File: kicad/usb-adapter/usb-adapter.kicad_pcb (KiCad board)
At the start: 2 copper layers, 17.2 x 40.9 mm, 3 parts, among them J1 USB-A plug, port A, J2 USB-A plug, port B, J3 To main board

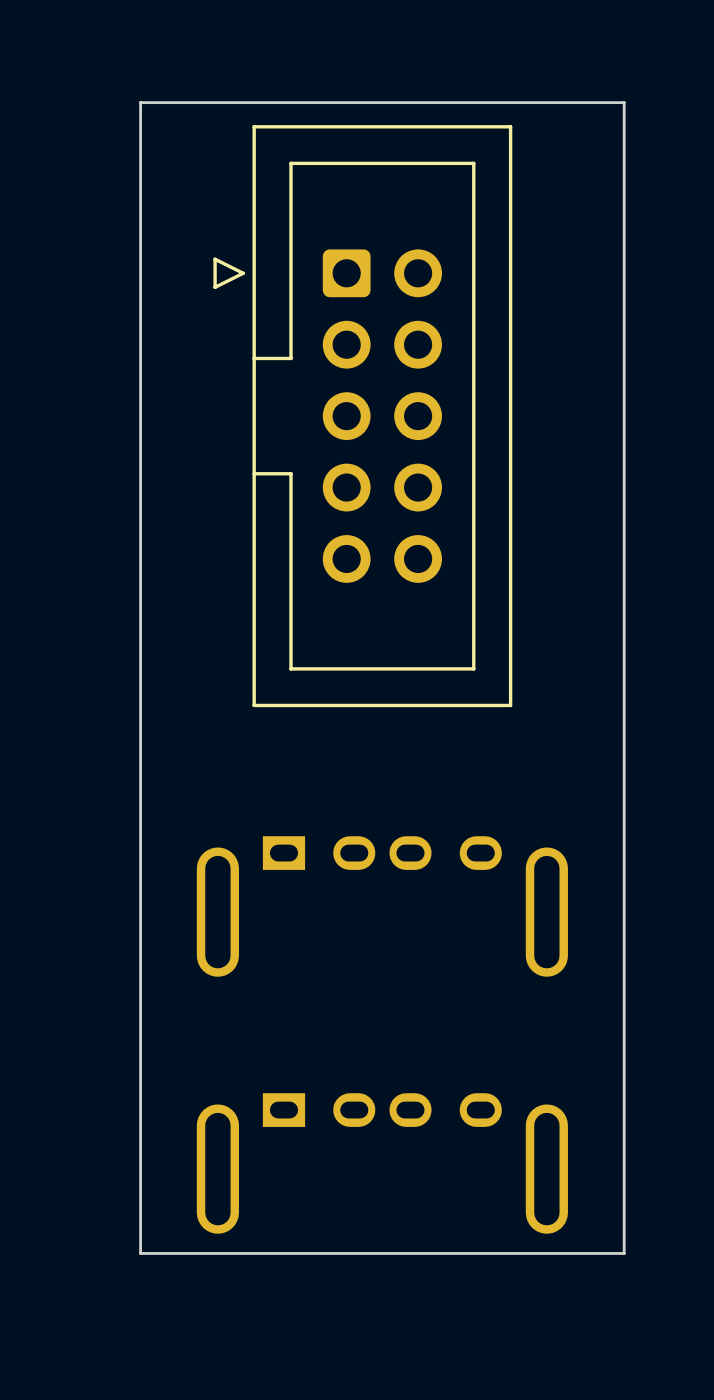
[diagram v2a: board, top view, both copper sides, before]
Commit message: USB adapters: routed board, plug placeholder, and both in Moirae's 3D
The adapter's plug tails sit on the plug's centre line (as routed); its
3D plug is a 12 x 4.5 x 15 mm box. The generator no longer overwrites the
hand-routed board. USBA1 / USBA2, board-only on the main board, stand the
adapter at the Pi 4's two USB stacks (27.0 and 9.0 up its port edge), plug
face 3 mm off the port faces.

Co-Authored-By: Claude Opus 5.5 <noreply@anthropic.com>
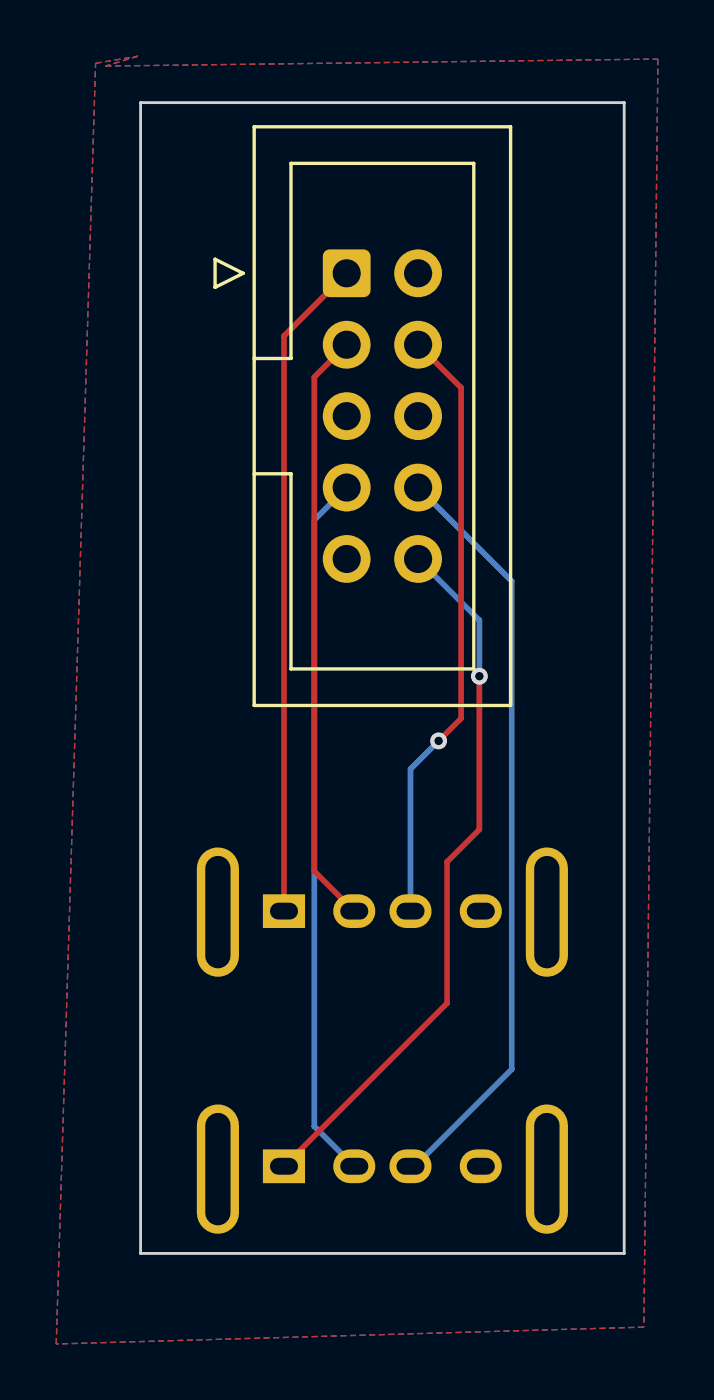
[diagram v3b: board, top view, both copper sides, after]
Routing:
- net /DP_B: track 0.00 -> 26.9 mm
- net /VBUS_B: track 0.00 -> 25.4 mm, vias 0 -> 1
- net /DM_B: track 0.00 -> 25.2 mm
- net /VBUS_A: track 0.00 -> 23.6 mm
- net /DP_A: track 0.00 -> 21.5 mm, vias 0 -> 1
- net /DM_A: track 0.00 -> 21.2 mm
- added copper zone on B.Cu, net GND
- added copper zone on F.Cu, net GND
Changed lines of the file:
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@@
 		)
 		(pad "1" thru_hole rect
-			(at -3.5 -2.1)
+			(at -3.5 -0.035)
 			(size 1.5 1.2)
 			(drill oval 1 0.6)
@@
 		)
 		(pad "2" thru_hole oval
-			(at -1 -2.1)
+			(at -1 -0.035)
 			(size 1.5 1.2)
 			(drill oval 1 0.6)
@@
 		)
 		(pad "3" thru_hole oval
-			(at 1 -2.1)
+			(at 1 -0.035)
 			(size 1.5 1.2)
 			(drill oval 1 0.6)
@@
 		)
 		(pad "4" thru_hole oval
-			(at 3.5 -2.1)
+			(at 3.5 -0.035)
 			(size 1.5 1.2)
 			(drill oval 1 0.6)
@@
 		)
 		(fp_text user "insert"
-			(at 0 -0.85 0)
+			(at 0 -1.2 0)
 			(layer "F.Fab")
 			(effects
@@
 		)
 		(pad "1" thru_hole rect
-			(at -3.5 -2.1)
+			(at -3.5 -0.1)
 			(size 1.5 1.2)
 			(drill oval 1 0.6)
@@
 		)
 		(pad "2" thru_hole oval
-			(at -1 -2.1)
+			(at -1 -0.1)
 			(size 1.5 1.2)
 			(drill oval 1 0.6)
@@
 		)
 		(pad "3" thru_hole oval
-			(at 1 -2.1)
+			(at 1 -0.1)
 			(size 1.5 1.2)
 			(drill oval 1 0.6)
@@
 		)
 		(pad "4" thru_hole oval
-			(at 3.5 -2.1)
+			(at 3.5 -0.1)
 			(size 1.5 1.2)
 			(drill oval 1 0.6)
@@
 			)
 		)
+	)
+	(segment
+		(start 98.73 60.769999)
+		(end 96.5 62.999999)
+		(width 0.2)
+		(layer "F.Cu")
+		(net "/VBUS_A")
+	)
+	(segment
+		(start 96.5 62.999999)
+		(end 96.5 83.455)
+		(width 0.2)
+		(layer "F.Cu")
+		(net "/VBUS_A")
+	)
+	(segment
+		(start 98.73 63.309999)
+		(end 97.58 64.459999)
+		(width 0.2)
+		(layer "F.Cu")
+		(net "/DM_A")
+	)
+	(segment
+		(start 97.58 64.459999)
+		(end 97.58 82.035)
+		(width 0.2)
+		(layer "F.Cu")
+		(net "/DM_A")
+	)
+	(segment
+		(start 97.58 82.035)
+		(end 99 83.455)
+		(width 0.2)
+		(layer "F.Cu")
+		(net "/DM_A")
+	)
+	(segment
+		(start 101.27 63.309999)
+		(end 102.8 64.839999)
+		(width 0.2)
+		(layer "F.Cu")
+		(net "/DP_A")
+	)
+	(segment
+		(start 102.8 64.839999)
+		(end 102.8 76.6)
+		(width 0.2)
+		(layer "F.Cu")
+		(net "/DP_A")
+	)
+	(segment
+		(start 102.8 76.6)
+		(end 102 77.4)
+		(width 0.2)
+		(layer "F.Cu")
+		(net "/DP_A")
+	)
+	(via
+		(at 102 77.4)
+		(size 0.6)
+		(drill 0.3)
+		(layers "F.Cu" "B.Cu")
+		(net "/DP_A")
+	)
+	(segment
+		(start 101 78.4)
+		(end 102 77.4)
+		(width 0.2)
+		(layer "B.Cu")
+		(net "/DP_A")
+	)
+	(segment
+		(start 101 83.455)
+		(end 101 78.4)
+		(width 0.2)
+		(layer "B.Cu")
+		(net "/DP_A")
+	)
+	(segment
+		(start 97.58 69.539999)
+		(end 97.58 91.11)
+		(width 0.2)
+		(layer "B.Cu")
+		(net "/DM_B")
+	)
+	(segment
+		(start 97.58 91.11)
+		(end 99 92.53)
+		(width 0.2)
+		(layer "B.Cu")
+		(net "/DM_B")
+	)
+	(segment
+		(start 98.73 68.389999)
+		(end 97.58 69.539999)
+		(width 0.2)
+		(layer "B.Cu")
+		(net "/DM_B")
+	)
+	(segment
+		(start 104.6 89.08)
+		(end 101.15 92.53)
+		(width 0.2)
+		(layer "B.Cu")
+		(net "/DP_B")
+	)
+	(segment
+		(start 101.27 68.389999)
+		(end 104.6 71.719999)
+		(width 0.2)
+		(layer "B.Cu")
+		(net "/DP_B")
+	)
+	(segment
+		(start 104.6 71.719999)
+		(end 104.6 89.08)
+		(width 0.2)
+		(layer "B.Cu")
+		(net "/DP_B")
+	)
+	(segment
+		(start 102.3 86.73)
+		(end 102.3 81.7)
+		(width 0.2)
+		(layer "F.Cu")
+		(net "/VBUS_B")
+	)
+	(segment
+		(start 96.5 92.53)
+		(end 102.3 86.73)
+		(width 0.2)
+		(layer "F.Cu")
+		(net "/VBUS_B")
+	)
+	(segment
+		(start 102.3 81.7)
+		(end 103.45 80.55)
+		(width 0.2)
+		(layer "F.Cu")
+		(net "/VBUS_B")
+	)
+	(segment
+		(start 103.45 80.55)
+		(end 103.45 75.1)
+		(width 0.2)
+		(layer "F.Cu")
+		(net "/VBUS_B")
+	)
+	(via
+		(at 103.45 75.1)
+		(size 0.6)
+		(drill 0.3)
+		(layers "F.Cu" "B.Cu")
+		(net "/VBUS_B")
+	)
+	(segment
+		(start 103.45 73.109999)
+		(end 103.45 75.1)
+		(width 0.2)
+		(layer "B.Cu")
+		(net "/VBUS_B")
+	)
+	(segment
+		(start 101.27 70.929999)
+		(end 103.45 73.109999)
+		(width 0.2)
+		(layer "B.Cu")
+		(net "/VBUS_B")
+	)
+	(zone
+		(net "GND")
+		(layers "F.Cu" "B.Cu")
+		(hatch edge 0.5)
+		(connect_pads
+			(clearance 0.5)
+		)
+		(min_thickness 0.25)
+		(fill yes
+			(thermal_gap 0.5)
+			(thermal_bridge_width 0.5)
+			(island_removal_mode 0)
+		)
+		(polygon
+			(pts
+				(xy 90.15 53.4) (xy 109.8 53.15) (xy 109.3 98.25) (xy 88.4 98.85) (xy 89.8 53.3) (xy 91.3 53.05)
+			)
+		)

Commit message: Pi USB ribbons routed on both boards; plug boxes in the adapter's 3D
Adapter J1 / J2 carry the 15 mm plug placeholder, and its STEP is
re-exported for Moirae. Pours refilled on both boards; the adapter's arc
approximation tightened so its pour clears the rounded edge.

Co-Authored-By: Claude Opus 5.5 <noreply@anthropic.com>
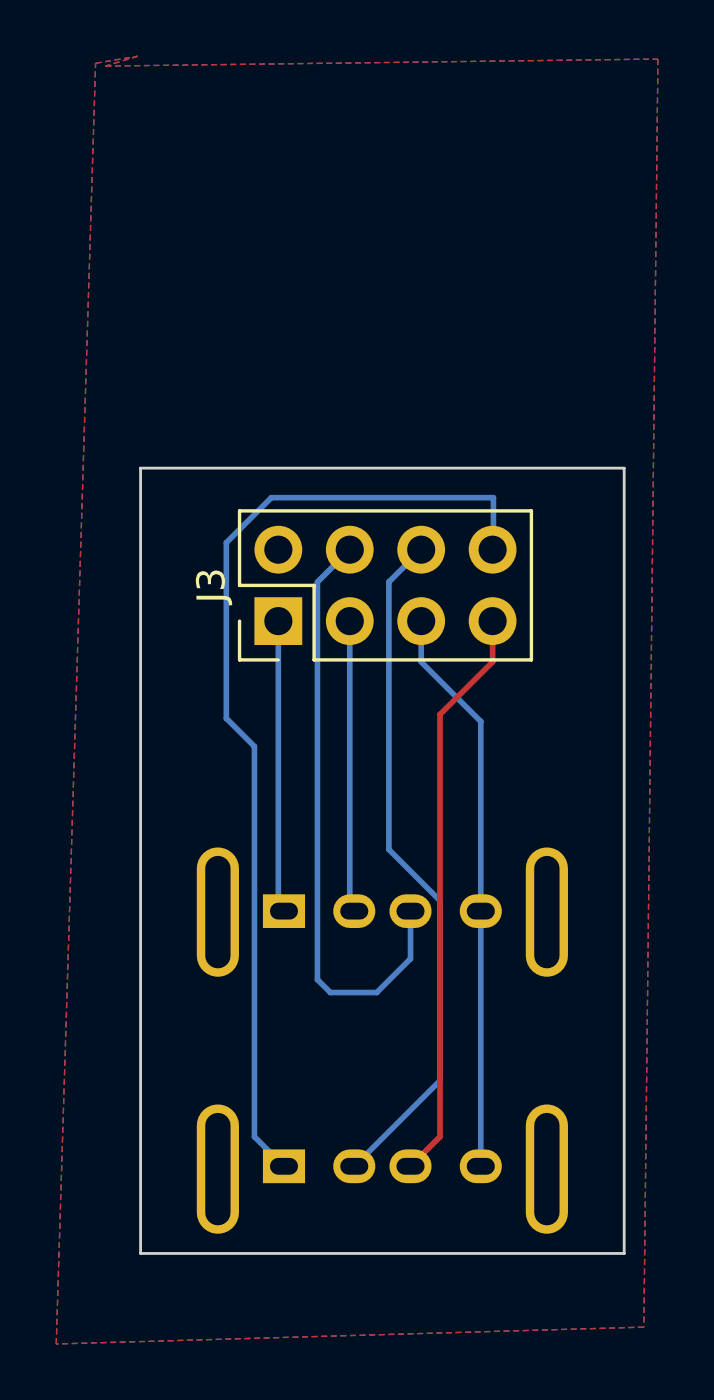
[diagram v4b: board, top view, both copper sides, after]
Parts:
- J3: footprint Connector_IDC:IDC-Header_2x05_P2.54mm_Vertical -> Connector_PinHeader_2.54mm:PinHeader_2x04_P2.54mm_Vertical
- moved J3 12.6 mm to (96.3, 73.1), turned to 90 degrees
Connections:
- J3 pad 6: GND -> /DM_B
- J3 pad 7: /DM_B -> /DP_B
- J3 pad 8: /DP_B -> /VBUS_B
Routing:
- net GND: track 0.00 -> 20.3 mm
- net /VBUS_A: track 23.6 -> 10.1 mm
- net /DM_A: track 21.2 -> 10.2 mm
- net /VBUS_B: track 25.4 -> 35.3 mm, vias 1 -> 0
- net /DP_B: track 26.9 -> 20.6 mm
- net /DM_B: track 25.2 -> 24.4 mm
- net /DP_A: vias 1 -> 0
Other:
- board size 17.2 x 40.9 mm -> 17.2 x 27.9 mm

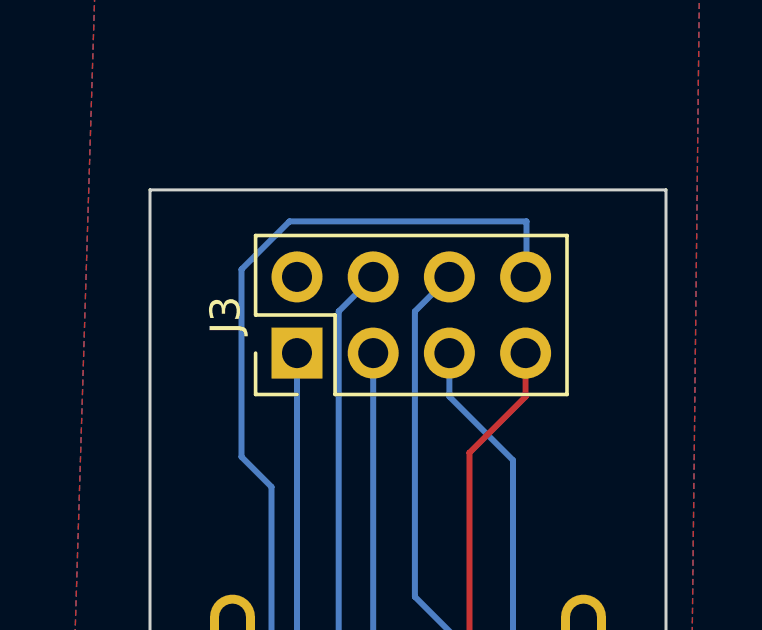
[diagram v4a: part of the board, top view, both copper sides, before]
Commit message: USB adapter: red-stripe marker at the header's pin 1-2 end
Co-Authored-By: Claude Opus 5.5 <noreply@anthropic.com>
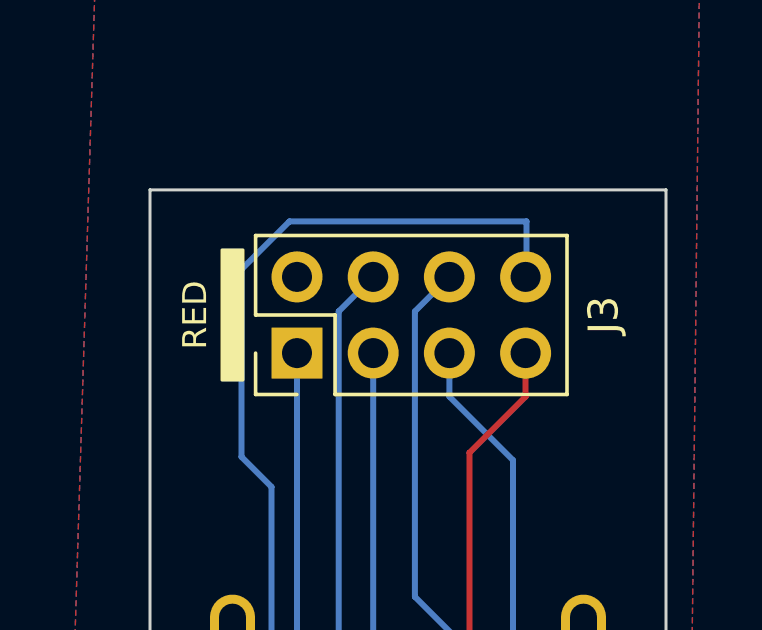
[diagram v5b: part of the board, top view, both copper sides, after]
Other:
- board text added: "RED"
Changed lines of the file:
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@@
 		(tags "Through hole pin header THT 2x04 2.54mm double row")
 		(property "Reference" "J3"
-			(at 1.27 -2.38 90)
+			(at 1.27 10.22 90)
 			(layer "F.SilkS")
 			(effects
@@
 		)
 	)
+	(gr_rect
+		(start 93.8 69.699999)
+		(end 94.5 74.04)
+		(stroke
+			(width 0.1)
+			(type default)
+		)
+		(fill yes)
+		(layer "F.SilkS")
+	)
 	(gr_line
 		(start 88.4 76.6)
@@
 		(layer "Edge.Cuts")
 	)
+	(gr_text "RED"
+		(at 92.899999 71.87 90)
+		(layer "F.SilkS")
+		(effects
+			(font
+				(size 0.8 0.8)
+				(thickness 0.12)
+			)
+		)
+	)
 	(gr_text "PI UNDERSIDE"
